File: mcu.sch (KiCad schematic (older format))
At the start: 34 parts, among them J4 Conn_01x04_Male, Q34 NX7002AK, SW21 SW_Push, SW22 SW_Push, U4 USBUF, U5 STM32F411RCT6, U7 LTV-357T, Y1 8MHz

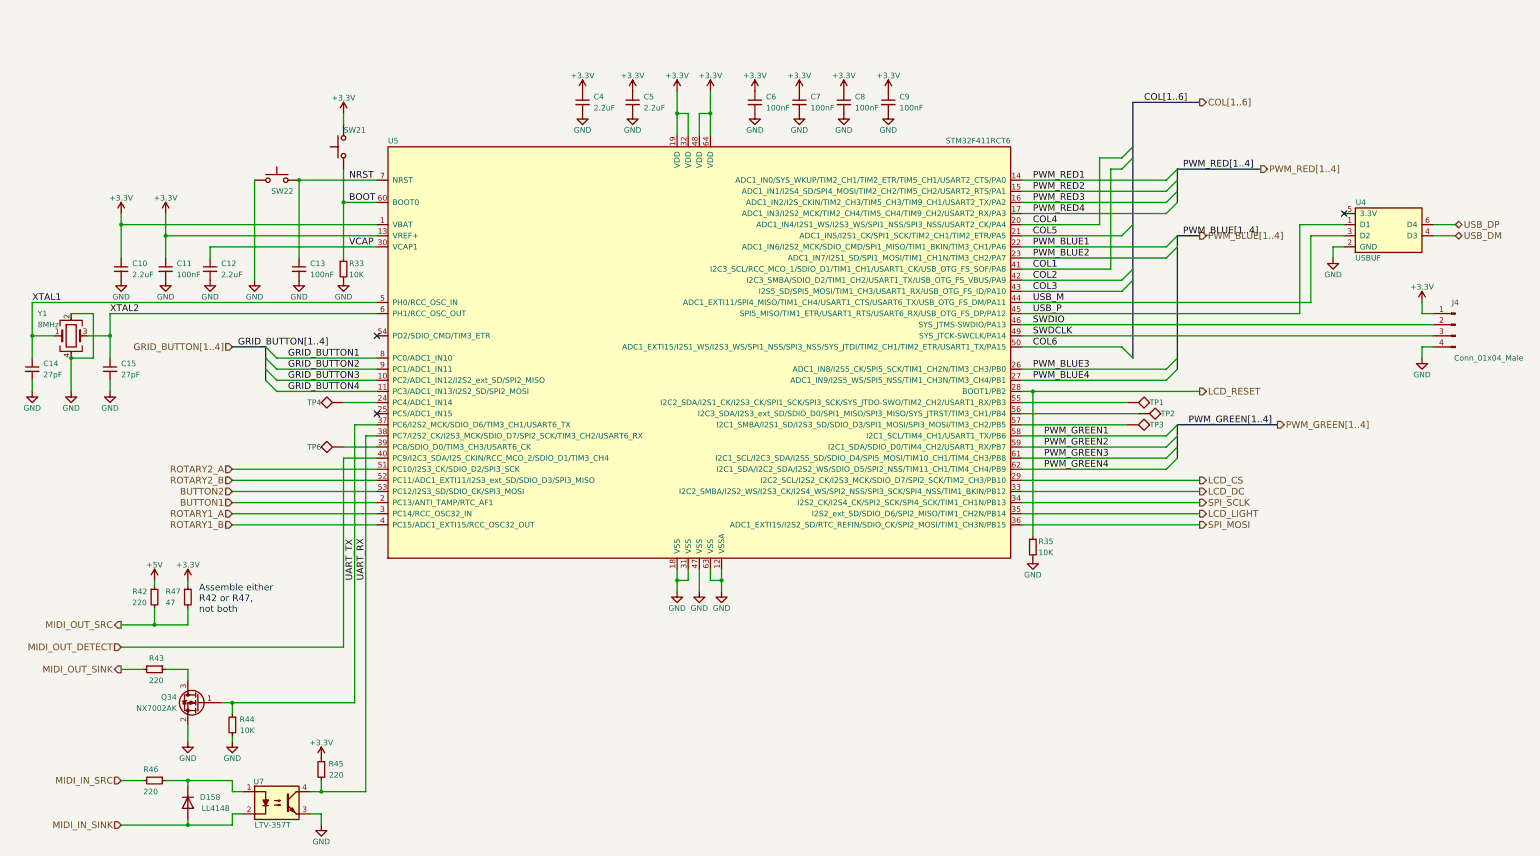
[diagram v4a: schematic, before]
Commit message: added logos to pcb
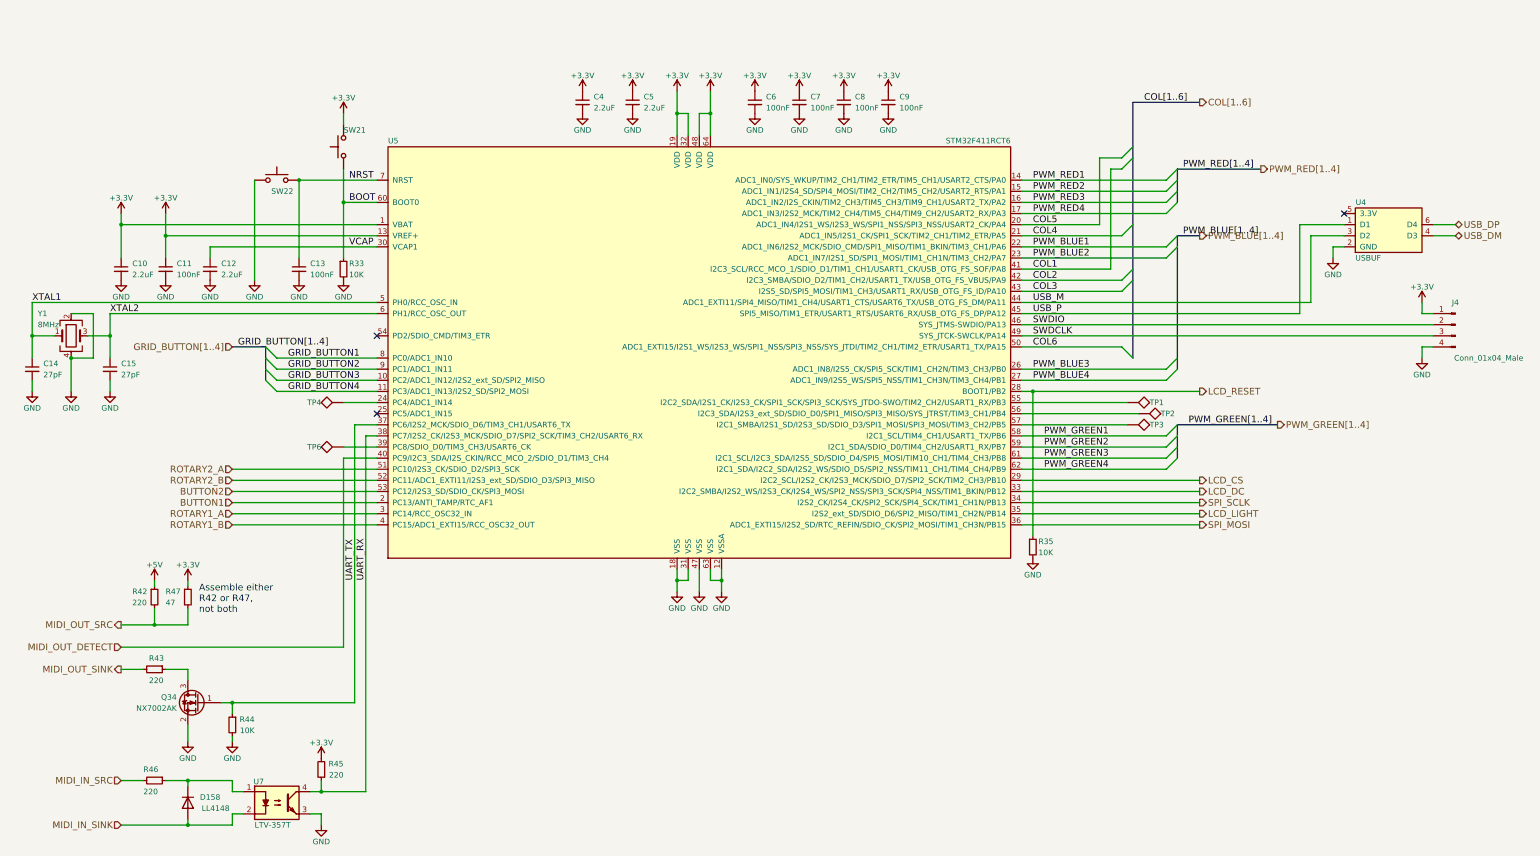
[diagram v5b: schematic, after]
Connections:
- net COL4: now also U5.21 (ADC1_IN5/I2S1_CK/SPI1_SCK/TIM2_CH1/TIM2_ETR/PA5); no longer U5.20 (ADC1_IN4/I2S1_WS/I2S3_WS/SPI1_NSS/SPI3_NSS/USART2_CK/PA4)
- net COL5: now also U5.20 (ADC1_IN4/I2S1_WS/I2S3_WS/SPI1_NSS/SPI3_NSS/USART2_CK/PA4); no longer U5.21 (ADC1_IN5/I2S1_CK/SPI1_SCK/TIM2_CH1/TIM2_ETR/PA5)
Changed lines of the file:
@@
 Text Label 11000 4450 0    60   ~ 0
 COL3
+Text Label 11000 3950 0    60   ~ 0
+COL4
 Text Label 11000 3850 0    60   ~ 0
-COL4
-Text Label 11000 3950 0    60   ~ 0
 COL5
 Text Label 11000 4950 0    60   ~ 0
@@
 	3900 9150 3800 9150
 Wire Wire Line
-	3800 9250 3800 9150
-Wire Wire Line
-	2800 9250 3800 9250
+	3800 9150 3800 9250
+Wire Wire Line
+	3800 9250 2800 9250
 Wire Wire Line
 	3400 9200 3400 9250
